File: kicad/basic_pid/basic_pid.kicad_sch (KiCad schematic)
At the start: 69 parts, among them J1 Input A, J2 Input B / Setpoint, J3 Output, J4 Output, SW1 SW_DPDT_x2, SW2 SW_DPDT_x2, SW3 SW_DPDT_x2, SW4 SW_SP4T, SW5 SW_DPDT_x2, SW6 SW_SP4T, SW7 SW_SP4T, SW8 SW_SP4T, SW9 SW_SP4T, U1 LM4040LP-5, U10 OPA189, U11 OPA189, U12 OPA189, U13 BUF634A, U2 LM4040LP-5, U3 LT1167, U4 LT1167, U5 OPA189, U6 OPA189, U7 OPA189, U8 BUF634A, U9 OPA189

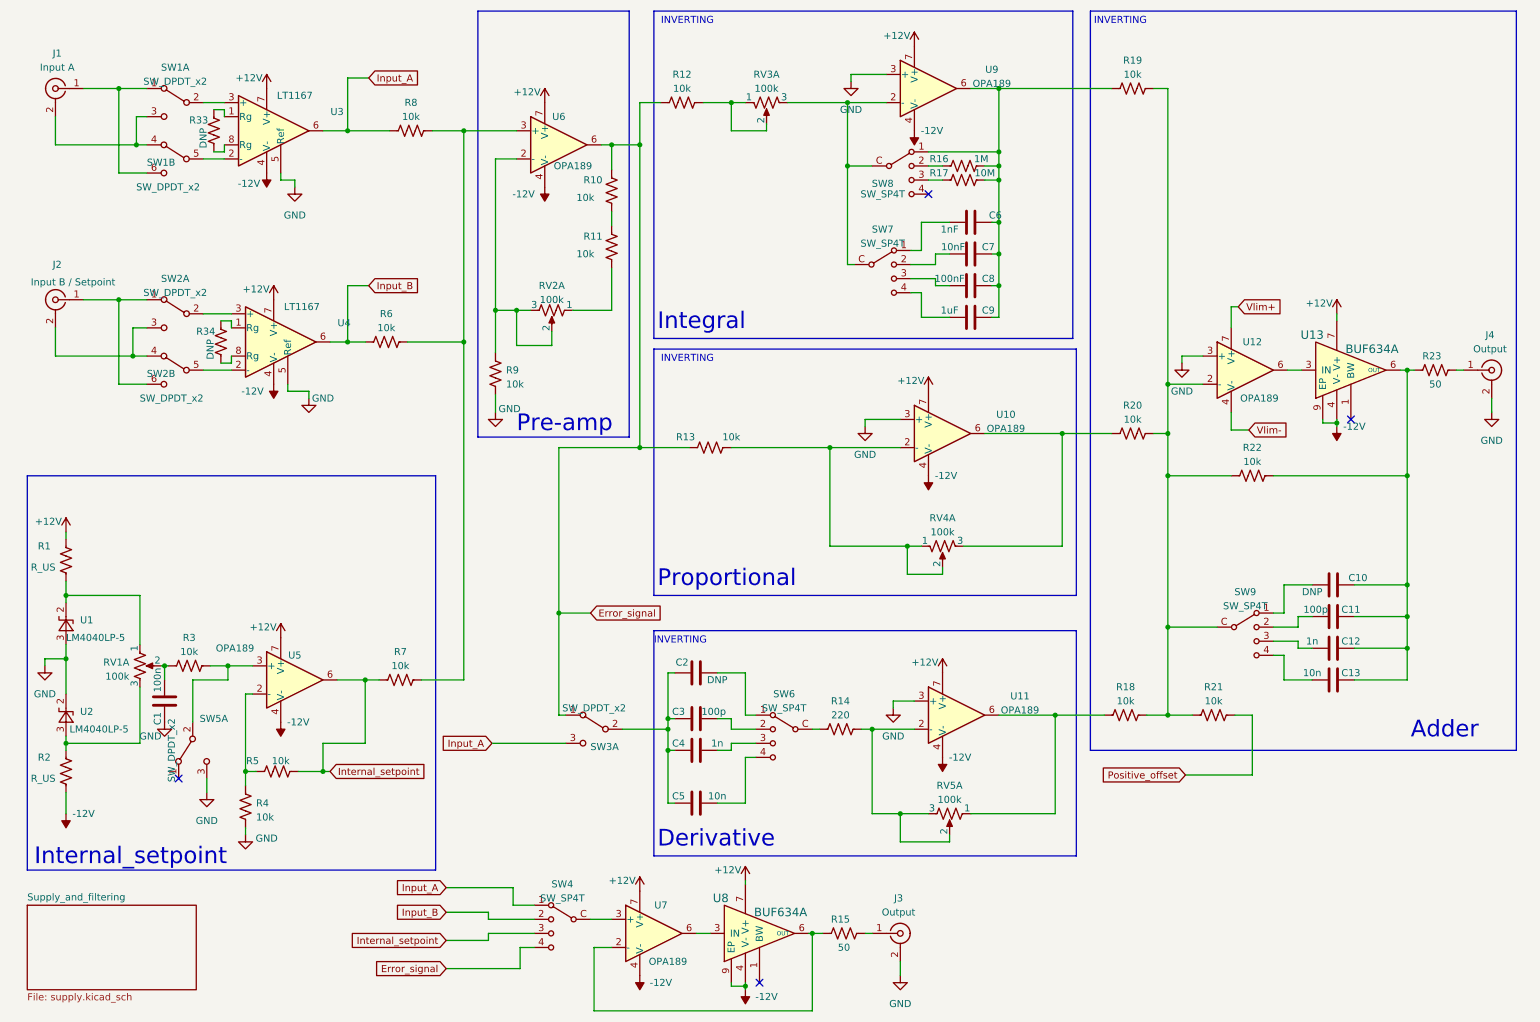
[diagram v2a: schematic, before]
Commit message: Layout almost completed
This is an almost completed snapshot of the layout. Here what to do:

1) Make sure that when flipped the back has sliders on the bottom: this will require
   reversing the direction of increasing gain with consequent shortening of certain
   signal traces

2) Fix the position of connectors, sliders and switches to "reasonable locations"
3) Make a verbose silkscreen (expecially on bottom) showing all functions.
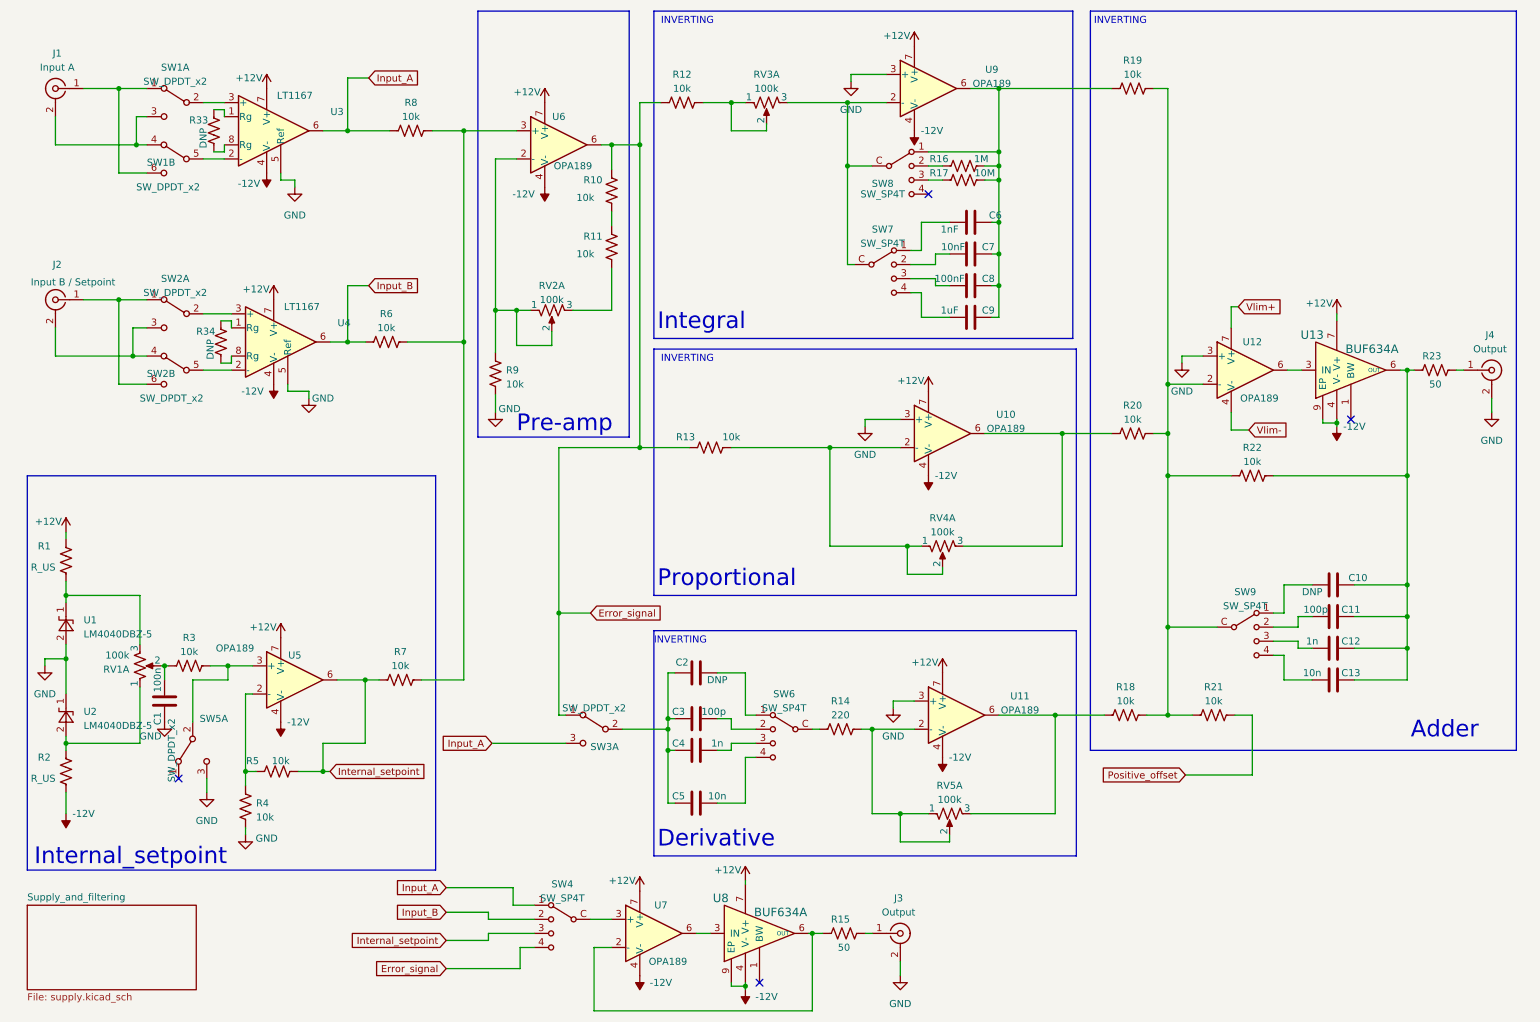
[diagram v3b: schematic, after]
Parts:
- removed U1, U2: LM4040LP-5, Package_TO_SOT_THT:TO-92_Inline, symbol Reference_Voltage:LM4040LP-5
- added U1, U2: LM4040DBZ-5, Package_TO_SOT_SMD:SOT-23, symbol Reference_Voltage:LM4040DBZ-5
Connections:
- net GND: now also U1.2 (A), U2.1 (K)
- net at RV1.1: now also R2.2, U2.2 (A); no longer R1.1
- net at RV1.3: now also R1.1, U1.1 (K); no longer R2.2
- net at R14.2, RV5.2, U11.2 (-): now also RV5.1; no longer RV5.3
- net at RV2.1: now also R9.2, RV2.2, U6.2 (-); no longer R11.1
- net at R18.1, U11.6: now also RV5.3; no longer RV5.1
- new net: R11.1, RV2.3
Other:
- moved on the sheet: RV2A, RV5A
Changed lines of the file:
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@@
     )
   )
-  (symbol (lib_id "local_lib:potentiometer_and _LED") (at 34.29 133.35 0) (unit 1)
-    (in_bom yes) (on_board yes) (dnp no) (fields_autoplaced)
-    (property "Reference" "RV1" (at 32.385 132.715 0)
+  (symbol (lib_id "local_lib:potentiometer_and _LED") (at 34.29 133.35 0) (mirror x) (unit 1)
+    (in_bom yes) (on_board yes) (dnp no)
+    (property "Reference" "RV1" (at 32.385 133.985 0)
       (effects (font (size 1.27 1.27)) (justify right))
     )
-    (property "Value" "100k" (at 32.385 135.255 0)
+    (property "Value" "100k" (at 32.385 131.445 0)
       (effects (font (size 1.27 1.27)) (justify right))
     )
@@
       (effects (font (size 1.27 1.27)) hide)
     )
-    (property "Datasheet" "https://www.bourns.com/docs/Product-Datasheets/PTL.pdf" (at 64.77 135.89 0)
-      (effects (font (size 1.27 1.27)) hide)
-    )
-    (property "PARTNO" "PTL45-15O0-104B1" (at 45.8121 140.4363 0)
-      (effects (font (size 1.27 1.27)) hide)
-    )
-    (property "DIGIKEY" "PTL45-15O0-104B1-ND" (at 47.8438 138.1568 0)
+    (property "Datasheet" "https://www.bourns.com/docs/Product-Datasheets/PTL.pdf" (at 64.77 130.81 0)
+      (effects (font (size 1.27 1.27)) hide)
+    )
+    (property "PARTNO" "PTL45-15O0-104B1" (at 45.8121 126.2637 0)
+      (effects (font (size 1.27 1.27)) hide)
+    )
+    (property "DIGIKEY" "PTL45-15O0-104B1-ND" (at 47.8438 128.5432 0)
       (effects (font (size 1.27 1.27)) hide)
     )
@@
     )
   )
-  (symbol (lib_id "local_lib:potentiometer_and _LED") (at 108.585 69.215 270) (unit 1)
+  (symbol (lib_id "Reference_Voltage:LM4040DBZ-5") (at 20.955 125.73 90) (unit 1)
     (in_bom yes) (on_board yes) (dnp no) (fields_autoplaced)
+    (property "Reference" "U1" (at 24.13 125.095 90)
+      (effects (font (size 1.27 1.27)) (justify right))
+    )
+    (property "Value" "LM4040DBZ-5" (at 24.13 127.635 90)
+      (effects (font (size 1.27 1.27)) (justify right))
+    )
+    (property "Footprint" "Package_TO_SOT_SMD:SOT-23" (at 26.035 125.73 0)
+      (effects (font (size 1.27 1.27) italic) hide)
+    )
+    (property "Datasheet" "http://www.ti.com/lit/ds/symlink/lm4040-n.pdf" (at 20.955 125.73 0)
+      (effects (font (size 1.27 1.27) italic) hide)
+    )
+    (property "PARTNO" "LM4040B50FTA" (at 20.955 125.73 90)
+      (effects (font (size 1.27 1.27)) hide)
+    )
+    (property "DIGIKEY" "LM4040B50FTADICT-ND" (at 20.955 125.73 90)
+      (effects (font (size 1.27 1.27)) hide)
+    )
+    (pin "1")
+    (pin "2")
+    (instances
+      (project "basic_pid"
+        (path "/3a3d7bcb-6fa5-41ef-9ea1-6d4ab7c492fd"
+          (reference "U1") (unit 1)
+        )
+      )
+    )
+  )
+  (symbol (lib_id "local_lib:potentiometer_and _LED") (at 108.585 69.215 90) (mirror x) (unit 1)
+    (in_bom yes) (on_board yes) (dnp no)
     (property "Reference" "RV2" (at 108.585 64.77 90)
       (effects (font (size 1.27 1.27)))
@@
       (effects (font (size 1.27 1.27)) hide)
     )
-    (property "Datasheet" "https://www.bourns.com/docs/Product-Datasheets/PTL.pdf" (at 106.045 99.695 0)
-      (effects (font (size 1.27 1.27)) hide)
-    )
-    (property "PARTNO" "PTL45-15O0-104B1" (at 101.4987 80.7371 0)
-      (effects (font (size 1.27 1.27)) hide)
-    )
-    (property "DIGIKEY" "PTL45-15O0-104B1-ND" (at 103.7782 82.7688 0)
+    (property "Datasheet" "https://www.bourns.com/docs/Product-Datasheets/PTL.pdf" (at 111.125 99.695 0)
+      (effects (font (size 1.27 1.27)) hide)
+    )
+    (property "PARTNO" "PTL45-15O0-104B1" (at 115.6713 80.7371 0)
+      (effects (font (size 1.27 1.27)) hide)
+    )
+    (property "DIGIKEY" "PTL45-15O0-104B1-ND" (at 113.3918 82.7688 0)
       (effects (font (size 1.27 1.27)) hide)
     )
@@
     )
   )
-  (symbol (lib_id "Reference_Voltage:LM4040LP-5") (at 20.955 142.24 90) (unit 1)
-    (in_bom yes) (on_board yes) (dnp no)
-    (property "Reference" "U2" (at 23.495 141.605 90)
-      (effects (font (size 1.27 1.27)) (justify right))
-    )
-    (property "Value" "LM4040LP-5" (at 21.59 144.78 90)
-      (effects (font (size 1.27 1.27)) (justify right))
-    )
-    (property "Footprint" "Package_TO_SOT_THT:TO-92_Inline" (at 26.035 142.24 0)
-      (effects (font (size 1.27 1.27) italic) hide)
-    )
-    (property "Datasheet" "http://www.ti.com/lit/ds/symlink/lm4040-n.pdf" (at 20.955 142.24 0)
-      (effects (font (size 1.27 1.27) italic) hide)
-    )
-    (pin "2")
-    (pin "3")
-    (instances
-      (project "basic_pid"
-        (path "/3a3d7bcb-6fa5-41ef-9ea1-6d4ab7c492fd"
-          (reference "U2") (unit 1)
-        )
-      )
-    )
-  )
   (symbol (lib_id "Device:C") (at 249.555 118.745 270) (mirror x) (unit 1)
     (in_bom yes) (on_board yes) (dnp no)
@@
     )
   )
-  (symbol (lib_id "local_lib:potentiometer_and _LED") (at 180.34 160.02 270) (unit 1)
-    (in_bom yes) (on_board yes) (dnp no) (fields_autoplaced)
+  (symbol (lib_id "local_lib:potentiometer_and _LED") (at 180.34 160.02 90) (mirror x) (unit 1)
+    (in_bom yes) (on_board yes) (dnp no)
     (property "Reference" "RV5" (at 180.34 154.94 90)
       (effects (font (size 1.27 1.27)))
@@
       (effects (font (size 1.27 1.27)) hide)
     )
-    (property "Datasheet" "https://www.bourns.com/docs/Product-Datasheets/PTL.pdf" (at 177.8 190.5 0)
-      (effects (font (size 1.27 1.27)) hide)
-    )
-    (property "PARTNO" "PTL45-15O0-104B1" (at 173.2537 171.5421 0)
-      (effects (font (size 1.27 1.27)) hide)
-    )
-    (property "DIGIKEY" "PTL45-15O0-104B1-ND" (at 175.5332 173.5738 0)
+    (property "Datasheet" "https://www.bourns.com/docs/Product-Datasheets/PTL.pdf" (at 182.88 190.5 0)
+      (effects (font (size 1.27 1.27)) hide)
+    )
+    (property "PARTNO" "PTL45-15O0-104B1" (at 187.4263 171.5421 0)
+      (effects (font (size 1.27 1.27)) hide)
+    )
+    (property "DIGIKEY" "PTL45-15O0-104B1-ND" (at 185.1468 173.5738 0)
       (effects (font (size 1.27 1.27)) hide)
     )
@@
         (path "/3a3d7bcb-6fa5-41ef-9ea1-6d4ab7c492fd"
           (reference "C4") (unit 1)
-        )
-      )
-    )
-  )
-  (symbol (lib_id "Reference_Voltage:LM4040LP-5") (at 20.955 125.73 90) (unit 1)
-    (in_bom yes) (on_board yes) (dnp no)
-    (property "Reference" "U1" (at 23.495 125.095 90)
-      (effects (font (size 1.27 1.27)) (justify right))
-    )
-    (property "Value" "LM4040LP-5" (at 20.955 128.27 90)
-      (effects (font (size 1.27 1.27)) (justify right))
-    )
-    (property "Footprint" "Package_TO_SOT_THT:TO-92_Inline" (at 26.035 125.73 0)
-      (effects (font (size 1.27 1.27) italic) hide)
-    )
-    (property "Datasheet" "http://www.ti.com/lit/ds/symlink/lm4040-n.pdf" (at 20.955 125.73 0)
-      (effects (font (size 1.27 1.27) italic) hide)
-    )
-    (pin "2")
-    (pin "3")
-    (instances
-      (project "basic_pid"
-        (path "/3a3d7bcb-6fa5-41ef-9ea1-6d4ab7c492fd"
-          (reference "U1") (unit 1)
         )
       )
@@
         )
       )
+    )
+  )
+  (symbol (lib_id "Reference_Voltage:LM4040DBZ-5") (at 20.955 142.24 90) (unit 1)
+    (in_bom yes) (on_board yes) (dnp no) (fields_autoplaced)
+    (property "Reference" "U2" (at 24.13 141.605 90)
+      (effects (font (size 1.27 1.27)) (justify right))
+    )
+    (property "Value" "LM4040DBZ-5" (at 24.13 144.145 90)
+      (effects (font (size 1.27 1.27)) (justify right))
+    )
+    (property "Footprint" "Package_TO_SOT_SMD:SOT-23" (at 26.035 142.24 0)
+      (effects (font (size 1.27 1.27) italic) hide)
+    )
+    (property "Datasheet" "http://www.ti.com/lit/ds/symlink/lm4040-n.pdf" (at 20.955 142.24 0)
+      (effects (font (size 1.27 1.27) italic) hide)
+    )
+    (property "PARTNO" "LM4040B50FTA" (at 20.955 142.24 90)
+      (effects (font (size 1.27 1.27)) hide)
+    )
+    (property "DIGIKEY" "LM4040B50FTADICT-ND" (at 20.955 142.24 90)
+      (effects (font (size 1.27 1.27)) hide)
+    )
+    (pin "1")
+    (pin "2")
+    (instances
+      (project "basic_pid"
+        (path "/3a3d7bcb-6fa5-41ef-9ea1-6d4ab7c492fd"
+          (reference "U2") (unit 1)
+        )
+      )

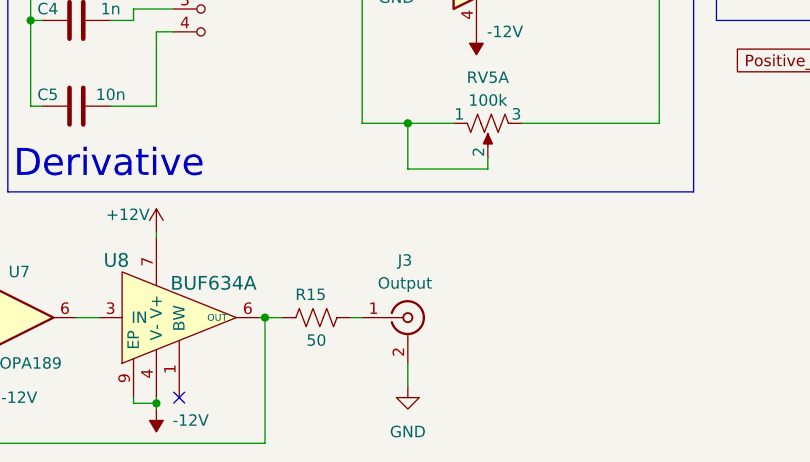
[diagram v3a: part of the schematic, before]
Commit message: Board is functionally operational but requires more reviews:
TO DO list
    1) Substitute input op-amps with an INA849: that should give higher bandwidth
    2) Make sure that when flipped the back has sliders on the bottom: this will require
       reversing the direction of increasing gain with consequent shortening of certain
       signal traces

    3) Fix the position of connectors, sliders and switches to "reasonable locations"
    4) Make a verbose silkscreen (expecially on bottom) showing all functions.
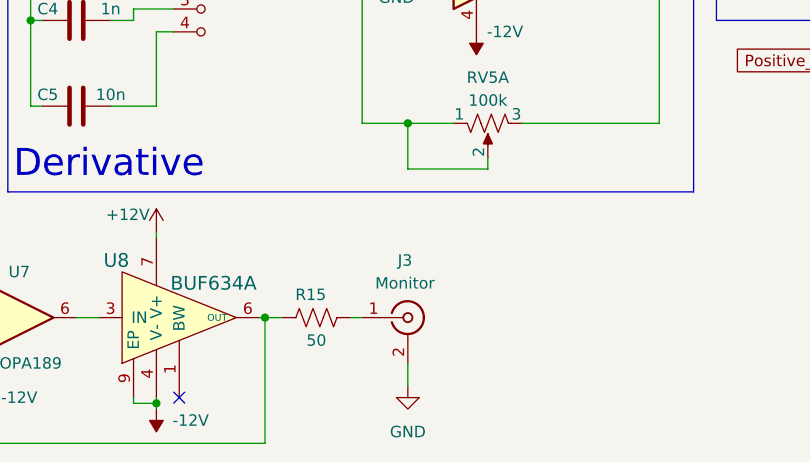
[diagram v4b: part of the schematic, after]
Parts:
- J3: value Output -> Monitor
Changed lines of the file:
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@@
       (effects (font (size 1.27 1.27)))
     )
-    (property "Value" "Output" (at 171.1326 177.8 0)
+    (property "Value" "Monitor" (at 171.1326 177.8 0)
       (effects (font (size 1.27 1.27)))
     )

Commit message: version sent to Advanced Circuits and OSHStencils
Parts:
- removed U3, U4: LT1167, Package_DIP:DIP-8_W7.62mm_LongPads, symbol Amplifier_Instrumentation:INA128
- added TP1, TP2, TP3: TestPoint, TestPoint:TestPoint_Pad_D3.0mm, symbol Connector:TestPoint
- added U3, U4: INA849, Package_SO:SOIC-8_3.9x4.9mm_P1.27mm, symbol Amplifier_Instrumentation:AD8236
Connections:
- net +12V: now also U3.8 (Vs+), U4.8 (Vs+)
- net -12V: now also U3.5 (Vs-), U4.5 (Vs-)
- net GND: now also U3.6 (Ref), U4.6 (Ref)
- net Input_A: now also U3.7
- net Input_B: now also U4.7
- net at SW2.2 (B): now also U4.1 (-)
- net at R2.2, U2.2 (A): now also RV1.3; no longer RV1.1
- net at R1.1, U1.1 (K): now also RV1.1; no longer RV1.3
- net at SW1.2 (B): now also U3.1 (-)
- net at SW2.5 (B): now also U4.4 (+)
- net at R18.1, RV5.3, U11.6: now also TP3.1
- net at R20.1, RV4.3, U10.6: now also TP2.1
- net at R33.1: now also U3.3 (Rg)
- net at R33.2: now also U3.2 (Rg)
- net at R34.1: now also U4.3 (Rg)
- net at R34.2: now also U4.2 (Rg)
- net at SW1.5 (B): now also U3.4 (+)
- net at C6.1, C7.1, C8.1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: now also TP1.1
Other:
- moved on the sheet: R6, R8
